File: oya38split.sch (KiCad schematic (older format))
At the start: 89 parts, among them U1 ProMicro

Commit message: added encoder
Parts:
- U1: footprint Keebio-Parts:ArduinoProMicro -> Keebio-Parts:ArduinoProMicro-ZigZag
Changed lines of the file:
@@
 F 0 "U1" H 3000 3987 60  0000 C CNN
 F 1 "ProMicro" H 3000 3881 60  0000 C CNN
-F 2 "Keebio-Parts:ArduinoProMicro" V 4050 650 60  0001 C CNN
+F 2 "Keebio-Parts:ArduinoProMicro-ZigZag" V 4050 650 60  0001 C CNN
 F 3 "" V 4050 650 60  0001 C CNN
 	1    3000 3150

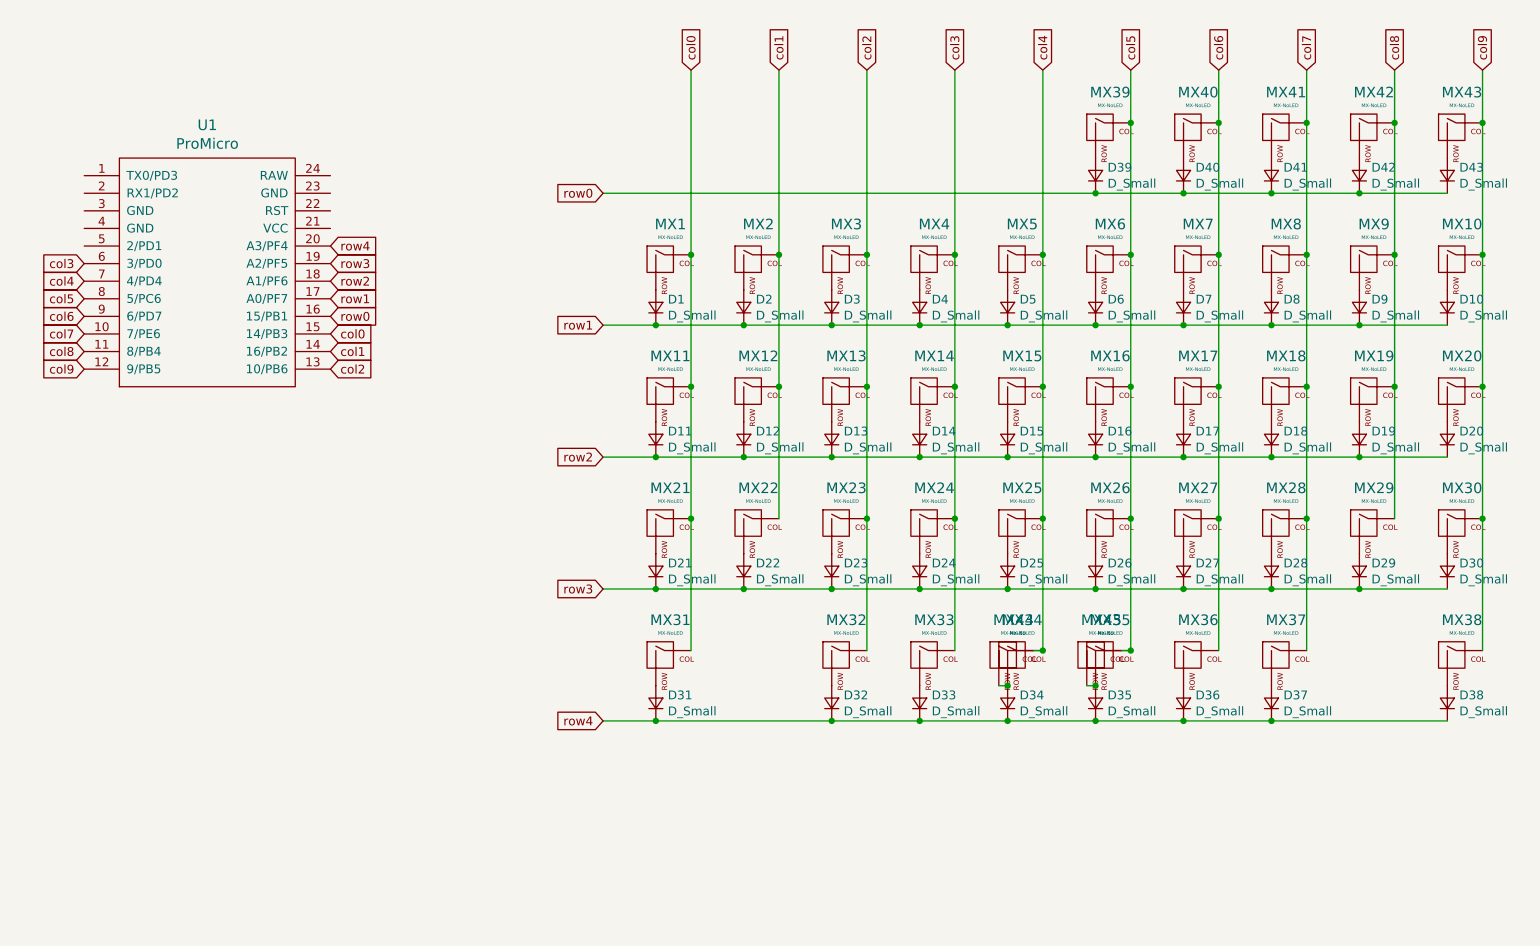
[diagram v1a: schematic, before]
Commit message: added rotary encoder
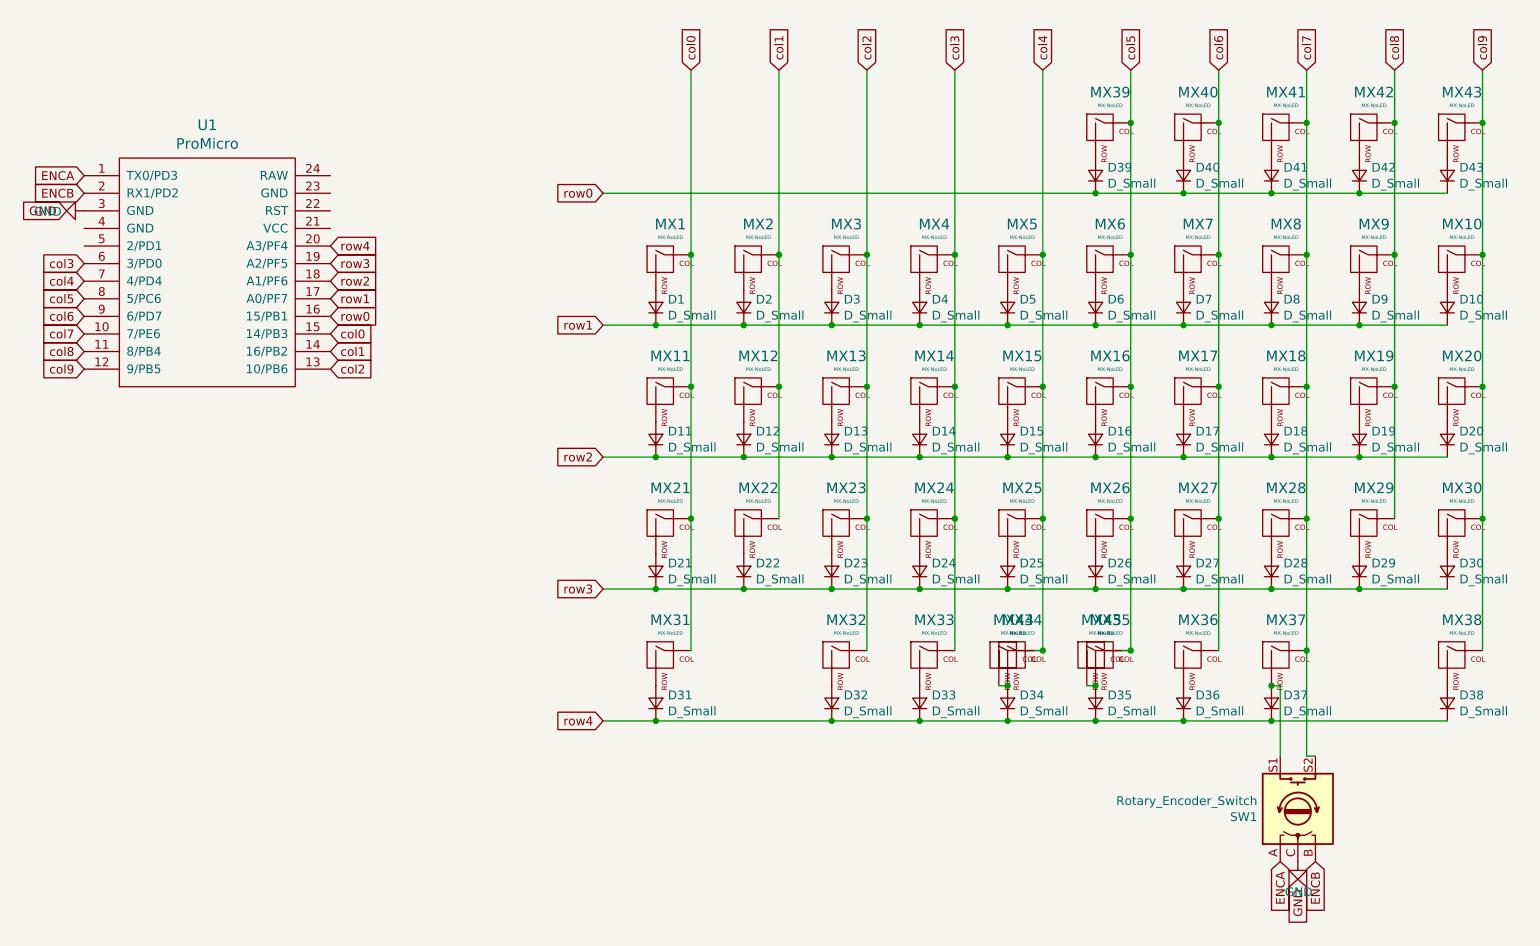
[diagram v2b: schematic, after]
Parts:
- added SW1: Rotary_Encoder_Switch, Keebio-Parts:RollerEncoder_Panasonic_EVQWGD001, symbol Device:Rotary_Encoder_Switch
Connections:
- net col7: now also SW1.S2
- net ENCA: now reaches U1.1 (TX0/PD3)
- net ENCA: now also SW1.A
- net ENCB: now reaches U1.2 (RX1/PD2)
- net ENCB: now also SW1.B
- net GND: now reaches U1.3 (GND)
- net GND: now also SW1.C
- net at D37.2 (A), MX37.2 (ROW): now also SW1.S1
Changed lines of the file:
@@
+	1    0    0    -1
+$EndComp
+$Comp
+L Device:Rotary_Encoder_Switch SW1
+U 1 1 61617C90
+P 9200 6200
+F 0 "SW1" V 9154 6430 50  0000 L CNN
+F 1 "Rotary_Encoder_Switch" V 9245 6430 50  0000 L CNN
+F 2 "Keebio-Parts:RollerEncoder_Panasonic_EVQWGD001" H 9050 6360 50  0001 C CNN
+F 3 "~" H 9200 6460 50  0001 C CNN
+	1    9200 6200
+	0    -1   -1   0
+$EndComp
+Wire Wire Line
+	9250 5300 9250 5900
+Wire Wire Line
+	9250 5900 9300 5900
+Connection ~ 9250 5300
+Wire Wire Line
+	9050 5500 9100 5500
+Wire Wire Line
+	9100 5500 9100 5900
+Connection ~ 9050 5500
+Text GLabel 9100 6500 3    50   Input ~ 0
+ENCA
+Text GLabel 9200 6600 3    50   Input ~ 0
+GND
+Text GLabel 9300 6500 3    50   Input ~ 0
+ENCB
+Text GLabel 2300 2600 0    50   Input ~ 0
+ENCA
+Text GLabel 2300 2700 0    50   Input ~ 0
+ENCB
+Text GLabel 2200 2800 0    50   Input ~ 0
+GND
+$Comp
+L power:GND #PWR0101
+U 1 1 6162DCD2
+P 2300 2800
+F 0 "#PWR0101" H 2300 2550 50  0001 C CNN
+F 1 "GND" V 2305 2672 50  0000 R CNN
+F 2 "" H 2300 2800 50  0001 C CNN
+F 3 "" H 2300 2800 50  0001 C CNN
+	1    2300 2800
+	0    1    1    0
+$EndComp
+$Comp
+L power:GND #PWR0102
+U 1 1 6163BD49
+P 9200 6500
+F 0 "#PWR0102" H 9200 6250 50  0001 C CNN
+F 1 "GND" H 9205 6327 50  0000 C CNN
+F 2 "" H 9200 6500 50  0001 C CNN
+F 3 "" H 9200 6500 50  0001 C CNN
+	1    9200 6500
 	1    0    0    -1
 $EndComp

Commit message: changing pcb
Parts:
- D1, D10, D11, D12, D13, D14, D15, D16, D17, D18, D19, D2, D20, D21, D22, D23, D24, D25, D26, D27, D28, D29, D3, D30, D31, D32, D33, D34, D35, D36, D37, D38, D39, D4, D40, D41, D42, D43, D5, D6, D7, D8, D9: footprint kbd:D3_SMD_v2 -> Keebio-Parts:D_0805
- MX1, MX10, MX11, MX12, MX13, MX14, MX15, MX16, MX17, MX18, MX19, MX2, MX20, MX21, MX22, MX23, MX24, MX25, MX26, MX27, MX28, MX29, MX3, MX30, MX31, MX32, MX33, MX34, MX35, MX36, MX37, MX38, MX39, MX4, MX40, MX41, MX42, MX43, MX5, MX6, MX7, MX8, MX9: footprint MX_Only:MXOnly-1U-NoLED -> MX_Only:MXOnly-1U-Hotswap
- MX44, MX45: footprint MX_Only:MXOnly-2U-ReversedStabilizers-NoLED -> MX_Only:MXOnly-2U-Hotswap

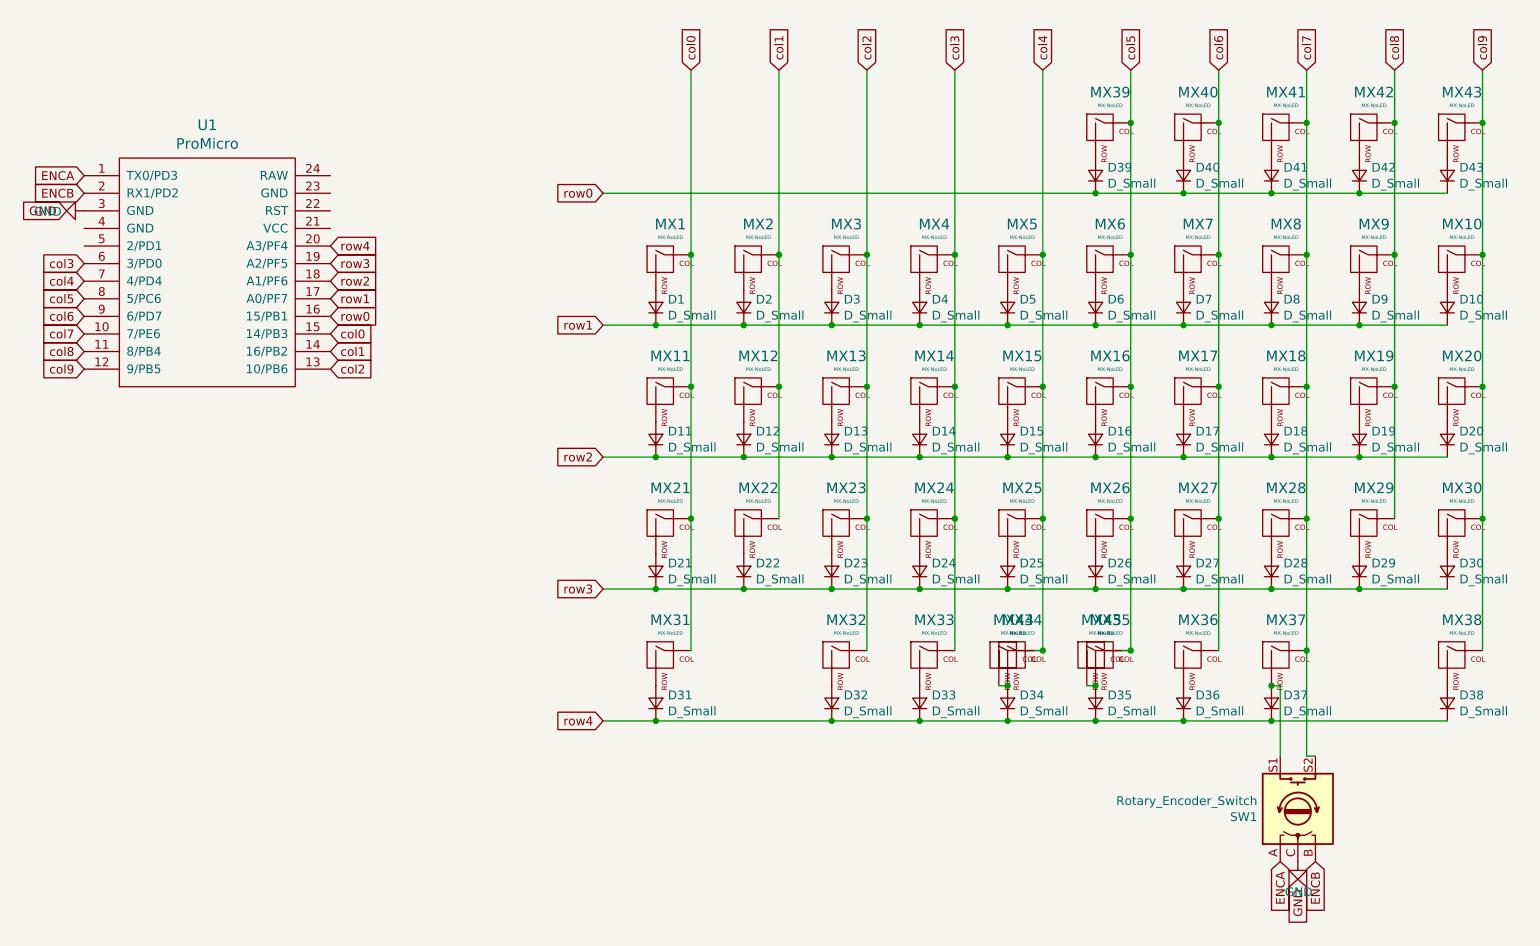
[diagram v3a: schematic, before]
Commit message: added choc support
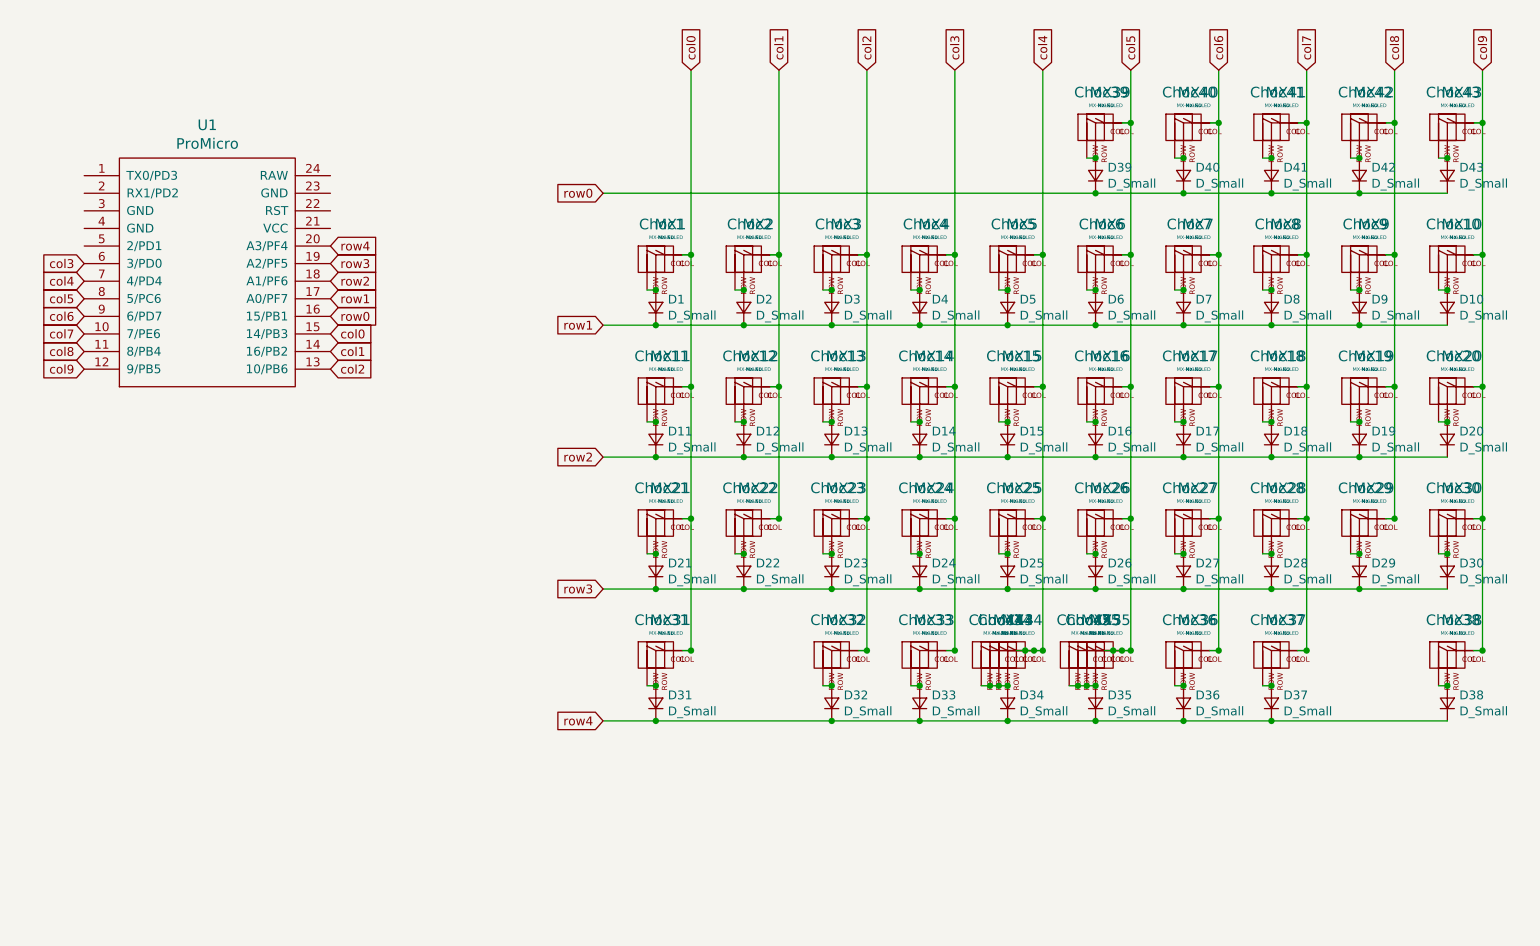
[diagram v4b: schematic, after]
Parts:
- removed SW1: Rotary_Encoder_Switch, Keebio-Parts:RollerEncoder_Panasonic_EVQWGD001, symbol Device:Rotary_Encoder_Switch
- added Choc1, Choc10, Choc11, Choc12, Choc13, Choc14, Choc15, Choc16, Choc17, Choc18, Choc19, Choc2, Choc20, Choc21, Choc22, Choc23, Choc24, Choc25, Choc26, Choc27, Choc28, Choc29, Choc3, Choc30, Choc31, Choc32, Choc33, Choc34, Choc35, Choc36, Choc37, Choc38, Choc39, Choc4, Choc40, Choc41, Choc42, Choc43, Choc44, Choc45, Choc5, Choc6, Choc7, Choc8, Choc9: MX-NoLED, kbd:ChocV1_V2_Hotswap, symbol MX_Alps_Hybrid:MX-NoLED
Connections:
- net col0: now also Choc1.1 (COL), Choc11.1 (COL), Choc21.1 (COL), Choc31.1 (COL)
- net col1: now also Choc12.1 (COL), Choc2.1 (COL), Choc22.1 (COL)
- net col2: now also Choc13.1 (COL), Choc23.1 (COL), Choc3.1 (COL), Choc32.1 (COL)
- net col3: now also Choc14.1 (COL), Choc24.1 (COL), Choc33.1 (COL), Choc4.1 (COL)
- net col4: now also Choc15.1 (COL), Choc25.1 (COL), Choc34.1 (COL), Choc44.1 (COL), Choc5.1 (COL)
- net col5: now also Choc16.1 (COL), Choc26.1 (COL), Choc35.1 (COL), Choc39.1 (COL), Choc45.1 (COL), Choc6.1 (COL)
- net col6: now also Choc17.1 (COL), Choc27.1 (COL), Choc36.1 (COL), Choc40.1 (COL), Choc7.1 (COL)
- net col7: now also Choc18.1 (COL), Choc28.1 (COL), Choc37.1 (COL), Choc41.1 (COL), Choc8.1 (COL)
- net col8: now also Choc19.1 (COL), Choc29.1 (COL), Choc42.1 (COL), Choc9.1 (COL)
- net col9: now also Choc10.1 (COL), Choc20.1 (COL), Choc30.1 (COL), Choc38.1 (COL), Choc43.1 (COL)
- net at D39.2 (A), MX39.2 (ROW): now also Choc39.2 (ROW)
- net at D40.2 (A), MX40.2 (ROW): now also Choc40.2 (ROW)
- net at D41.2 (A), MX41.2 (ROW): now also Choc41.2 (ROW)
- net at D42.2 (A), MX42.2 (ROW): now also Choc42.2 (ROW)
- net at D43.2 (A), MX43.2 (ROW): now also Choc43.2 (ROW)
- net at D1.2 (A), MX1.2 (ROW): now also Choc1.2 (ROW)
- net at D2.2 (A), MX2.2 (ROW): now also Choc2.2 (ROW)
- net at D3.2 (A), MX3.2 (ROW): now also Choc3.2 (ROW)
- net at D4.2 (A), MX4.2 (ROW): now also Choc4.2 (ROW)
- net at D5.2 (A), MX5.2 (ROW): now also Choc5.2 (ROW)
- net at D6.2 (A), MX6.2 (ROW): now also Choc6.2 (ROW)
- net at D7.2 (A), MX7.2 (ROW): now also Choc7.2 (ROW)
- net at D8.2 (A), MX8.2 (ROW): now also Choc8.2 (ROW)
- net at D9.2 (A), MX9.2 (ROW): now also Choc9.2 (ROW)
- net at D10.2 (A), MX10.2 (ROW): now also Choc10.2 (ROW)
- net at D11.2 (A), MX11.2 (ROW): now also Choc11.2 (ROW)
- net at D12.2 (A), MX12.2 (ROW): now also Choc12.2 (ROW)
- net at D13.2 (A), MX13.2 (ROW): now also Choc13.2 (ROW)
- net at D14.2 (A), MX14.2 (ROW): now also Choc14.2 (ROW)
- net at D15.2 (A), MX15.2 (ROW): now also Choc15.2 (ROW)
- net at D16.2 (A), MX16.2 (ROW): now also Choc16.2 (ROW)
- net at D17.2 (A), MX17.2 (ROW): now also Choc17.2 (ROW)
- net at D18.2 (A), MX18.2 (ROW): now also Choc18.2 (ROW)
- net at D19.2 (A), MX19.2 (ROW): now also Choc19.2 (ROW)
- net at D20.2 (A), MX20.2 (ROW): now also Choc20.2 (ROW)
- net at D21.2 (A), MX21.2 (ROW): now also Choc21.2 (ROW)
- net at D22.2 (A), MX22.2 (ROW): now also Choc22.2 (ROW)
- net at D23.2 (A), MX23.2 (ROW): now also Choc23.2 (ROW)
- net at D24.2 (A), MX24.2 (ROW): now also Choc24.2 (ROW)
- net at D25.2 (A), MX25.2 (ROW): now also Choc25.2 (ROW)
- net at D26.2 (A), MX26.2 (ROW): now also Choc26.2 (ROW)
- net at D27.2 (A), MX27.2 (ROW): now also Choc27.2 (ROW)
- net at D28.2 (A), MX28.2 (ROW): now also Choc28.2 (ROW)
- net at D29.2 (A), MX29.2 (ROW): now also Choc29.2 (ROW)
- net at D30.2 (A), MX30.2 (ROW): now also Choc30.2 (ROW)
- net at D31.2 (A), MX31.2 (ROW): now also Choc31.2 (ROW)
- net at D33.2 (A), MX33.2 (ROW): now also Choc33.2 (ROW)
- net at D34.2 (A), MX34.2 (ROW), MX44.2 (ROW): now also Choc34.2 (ROW), Choc44.2 (ROW)
- net at D35.2 (A), MX35.2 (ROW), MX45.2 (ROW): now also Choc35.2 (ROW), Choc45.2 (ROW)
- net at D36.2 (A), MX36.2 (ROW): now also Choc36.2 (ROW)
- net at D38.2 (A), MX38.2 (ROW): now also Choc38.2 (ROW)
- net at D32.2 (A), MX32.2 (ROW): now also Choc32.2 (ROW)
- net at D37.2 (A), MX37.2 (ROW): now also Choc37.2 (ROW)
- net ENCA: no longer names the net of U1.1 (TX0/PD3)
- net ENCB: no longer names the net of U1.2 (RX1/PD2)
- net GND: no longer names the net of U1.3 (GND)
